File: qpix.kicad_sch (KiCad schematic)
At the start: 91 parts, among them J1 Conn_01x40, J10 VC, J13 DigReset, J2 Conn_01x09, J3 Conn_02x03, J4 Conn_02x03, J5 SPI, J6 Conn_02x03, J8 Conn_02x03, J9 Conn_Coaxial_Power, Q1 AO7400, Q2 AO7400, Q3 AO7400, Q4 AO7400, U1 qpix_digital

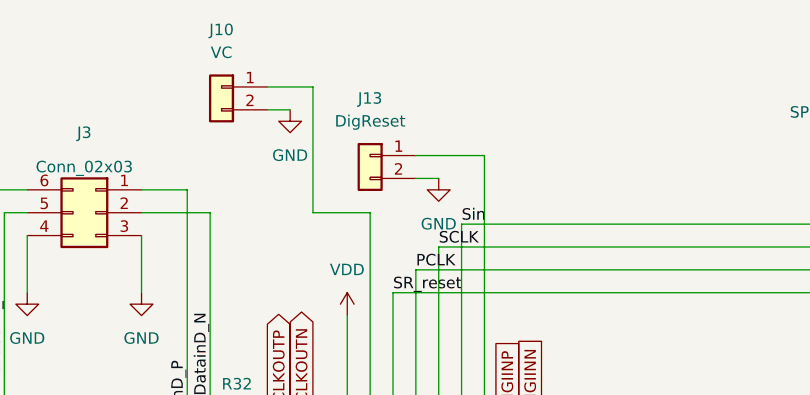
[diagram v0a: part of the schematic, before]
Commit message: clk select related components moved to the top layer
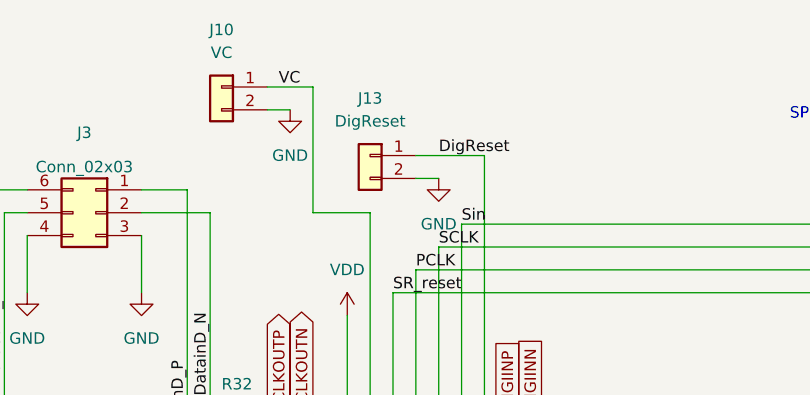
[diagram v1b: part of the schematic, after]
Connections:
- net DigReset: now reaches J13.1 (Pin_1), U1.122 (DigReset)
- net VC: now reaches J10.1 (Pin_1), U1.117 (VC)
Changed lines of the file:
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@@
+    (effects (font (size 1.27 1.27)) (justify left bottom))
+  )
+  (label "DigReset" (at 203.2 31.75 0) (fields_autoplaced)
     (effects (font (size 1.27 1.27)) (justify left bottom))
   )
@@
     (effects (font (size 1.27 1.27)) (justify left bottom))
   )
+  (label "VC" (at 185.42 24.13 0) (fields_autoplaced)
+    (effects (font (size 1.27 1.27)) (justify left bottom))
+  )

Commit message: replace led footprints with 0603, add power up led
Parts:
- D1, D2, D3, D4: footprint LED_SMD:LED_0201_0603Metric -> LED_SMD:LED_0603_1608Metric_Pad1.05x0.95mm_HandSolder
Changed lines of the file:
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@@
       (effects (font (size 1.27 1.27)) (justify right))
     )
-    (property "Footprint" "LED_SMD:LED_0201_0603Metric" (at 388.62 184.15 0)
+    (property "Footprint" "LED_SMD:LED_0603_1608Metric_Pad1.05x0.95mm_HandSolder" (at 388.62 184.15 0)
       (effects (font (size 1.27 1.27)) hide)
     )
@@
       (effects (font (size 1.27 1.27)) (justify right))
     )
-    (property "Footprint" "LED_SMD:LED_0201_0603Metric" (at 374.65 184.15 0)
+    (property "Footprint" "LED_SMD:LED_0603_1608Metric_Pad1.05x0.95mm_HandSolder" (at 374.65 184.15 0)
       (effects (font (size 1.27 1.27)) hide)
     )
@@
       (effects (font (size 1.27 1.27)) (justify right))
     )
-    (property "Footprint" "LED_SMD:LED_0201_0603Metric" (at 359.41 184.15 0)
+    (property "Footprint" "LED_SMD:LED_0603_1608Metric_Pad1.05x0.95mm_HandSolder" (at 359.41 184.15 0)
       (effects (font (size 1.27 1.27)) hide)
     )
@@
       (effects (font (size 1.27 1.27)) (justify right))
     )
-    (property "Footprint" "LED_SMD:LED_0201_0603Metric" (at 344.17 184.15 0)
-      (effects (font (size 1.27 1.27)) hide)
-    )
+    (property "Footprint" "LED_SMD:LED_0603_1608Metric_Pad1.05x0.95mm_HandSolder" (at 344.17 184.15 0)
+      (effects (font (size 1.27 1.27)) hide)
+    )

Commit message: start rework with lvds txrx :
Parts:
- added JP11, JP13: Jumper_2_Open, symbol Jumper:Jumper_2_Open
- added R48: 100, Resistor_SMD:R_0603_1608Metric, symbol Device:R_Small_US
- added U5: FIN1019M, Package_SO:SOIC-14_3.9x8.7mm_P1.27mm, symbol Interface:FIN1019M
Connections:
- net DatinA_N: now also JP11.2 (B), R48.1, U5.11 (DO-); no longer J4.2 (Pin_2)
- net DatinA_P: now also JP13.1 (A), JP13.2 (B), R48.2, U5.12 (DO+), U5.2 (DI)
- net DatoutA_N: no longer J4.6 (Pin_6)
- net DatoutA_P: no longer J4.5 (Pin_5)
- new net: J4.2 (Pin_2), JP11.1 (A)
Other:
- moved on the sheet: J4

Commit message: lvds receiver/driver added for every endeavour port along with 3.3V power supply
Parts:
- removed C22, C23: 100nF, Capacitor_SMD:C_0603_1608Metric, symbol Device:C
- removed J1: Conn_01x40, Connector_PinHeader_2.54mm:PinHeader_2x20_P2.54mm_Vertical, symbol Connector_Generic:Conn_01x40
- removed J2: Conn_01x09, Connector_PinHeader_2.54mm:PinHeader_1x09_P2.54mm_Vertical, symbol Connector_Generic:Conn_01x09
- removed J3, J4, J6, J8: Conn_02x03, Connector_PinSocket_2.54mm:PinSocket_2x03_P2.54mm_Horizontal, symbol Connector_Generic:Conn_02x03_Counter_Clockwise
- removed J9: Conn_Coaxial_Power, Connector_Coaxial:SMA_Amphenol_901-144_Vertical, symbol Connector:Conn_Coaxial_Power
- removed JP10, JP12, JP2, JP3, JP4, JP5, JP6, JP7, JP8, JP9: (no value), Connector_PinHeader_2.54mm:PinHeader_1x02_P2.54mm_Vertical, symbol Jumper:Jumper_2_Open
- removed JP11, JP13: Jumper_2_Open, symbol Jumper:Jumper_2_Open
- removed R1, R11, R12, R2, R3, R4, R5, R6: 10k, Resistor_SMD:R_0603_1608Metric, symbol Device:R_US
- removed R10, R14: 22k, Resistor_SMD:R_0603_1608Metric, symbol Device:R_Small_US
- removed R31, R32, R33, R35, R48: 100, Resistor_SMD:R_0603_1608Metric, symbol Device:R_Small_US
- removed U5: FIN1019M, Package_SO:SOIC-14_3.9x8.7mm_P1.27mm, symbol Interface:FIN1019M
- added C28: C, Capacitor_SMD:C_0603_1608Metric, symbol Device:C
- added R50, R67: NC, Resistor_SMD:R_0805_2012Metric_Pad1.20x1.40mm_HandSolder, symbol Device:R_Small_US
- added R54, R58, R62, R66: 100, Resistor_SMD:R_0805_2012Metric_Pad1.20x1.40mm_HandSolder, symbol Device:R_Small_US
- added R68, R69: 10k, Resistor_SMD:R_0603_1608Metric, symbol Device:R_US
- added SW1: SW_Push, Button_Switch_THT:SW_PUSH_6mm_H5mm, symbol Switch:SW_Push
- added TP1: TestInterr, TestPoint:TestPoint_Loop_D3.80mm_Drill2.0mm, symbol Connector:TestPoint
- added TP3, TP4, TP5, TP6: TestGnd, TestPoint:TestPoint_Loop_D3.80mm_Drill2.0mm, symbol Connector:TestPoint
- Q1, Q2, Q3, Q4: footprint Package_TO_SOT_SMD:SOT-323_SC-70 -> Package_TO_SOT_SMD:SOT-323_SC-70_Handsoldering
- renumbered C4 to C1, C13 to C10, C14 to C11, C15 to C12, C16 to C13, C17 to C14, C18 to C15, C24 to C16, C5 to C2, C6 to C3, C7 to C4, C8 to C5, C9 to C6, C10 to C7, C11 to C8, C12 to C9, J10 to J3, J13 to J4, R15 to R1, R24 to R10, R25 to R11, R26 to R12, R27 to R13, R28 to R14, R29 to R15, R30 to R16, R36 to R17, R37 to R18, R38 to R19, R16 to R2, R39 to R20, R40 to R21, R41 to R22, R42 to R23, R43 to R24, R44 to R25, R45 to R26, R17 to R3, R65 to R32, R66 to R37, R67 to R39, R18 to R4, R68 to R40, R19 to R5, R20 to R6, R21 to R7, R22 to R8, R23 to R9
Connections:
- net CLKDIGIINN: now also R50.2
- net CLKDIGIINP: now also R50.1
- net CLKOUTN: now also R67.1
- net CLKOUTP: now also R67.2
- net DatinA_N: now also R54.1
- net DatinA_P: now also R54.2
- net DatinB_N: now also R58.1
- net DatinB_P: now also R58.2
- net DigReset: now also C28.1, R68.2
- net GND: now also C28.2, R69.2, TP3.1, TP4.1, TP5.1, TP6.1
- net VDD: now also SW1.1
- net dbgInterr: now also TP1.1
- net +5V renamed VCC
- net DatainC_N renamed DatinC_N
- net DatinC_N: now also R62.2
- net DatainC_P renamed DatinC_P
- net DatinC_P: now also R62.1
- net DatainD_N renamed DatinD_N
- net DatinD_N: now also R66.2
- net DatainD_P renamed DatinD_P
- net DatinD_P: now also R66.1
- net DataoutC_N renamed DatoutC_N
- net DataoutC_P renamed DatoutC_P
- net DataoutD_N renamed DatoutD_N
- net DataoutD_P renamed DatoutD_P
- new net: R68.1, R69.1, SW1.2
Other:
- added sheet connectors (connectors.kicad_sch)
- added sheet portA (port.kicad_sch)
- added sheet portB (port.kicad_sch)
- added sheet portC (port.kicad_sch)
- added sheet portD (port.kicad_sch)
- note removed: "10k-22k"
- note removed: "2 22 uF 2 2.2 uf 2 220 nf 2 2nf"
- note removed: "Configuration jumpers"
- note removed: "Enable/disable Endevour transceivers"
- note removed: "Endeavor transceivers scaling factor 3 bits"
- note removed: "External interrogation"
- note removed: "Kurtis: One extra suggestion is that as you connect that output VDD to the chip, you can add some small series resistors (1 Ohm or less) so we can measure current draw on core voltages vs. IO voltages."
- note removed: "Q-Pix reset singnals from analog component"
- note removed: "TODO: add a power LED"
- moved on the sheet: C1, C10, C11, C12, C13, C14, C15, C16, C2, C3, C4, C5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

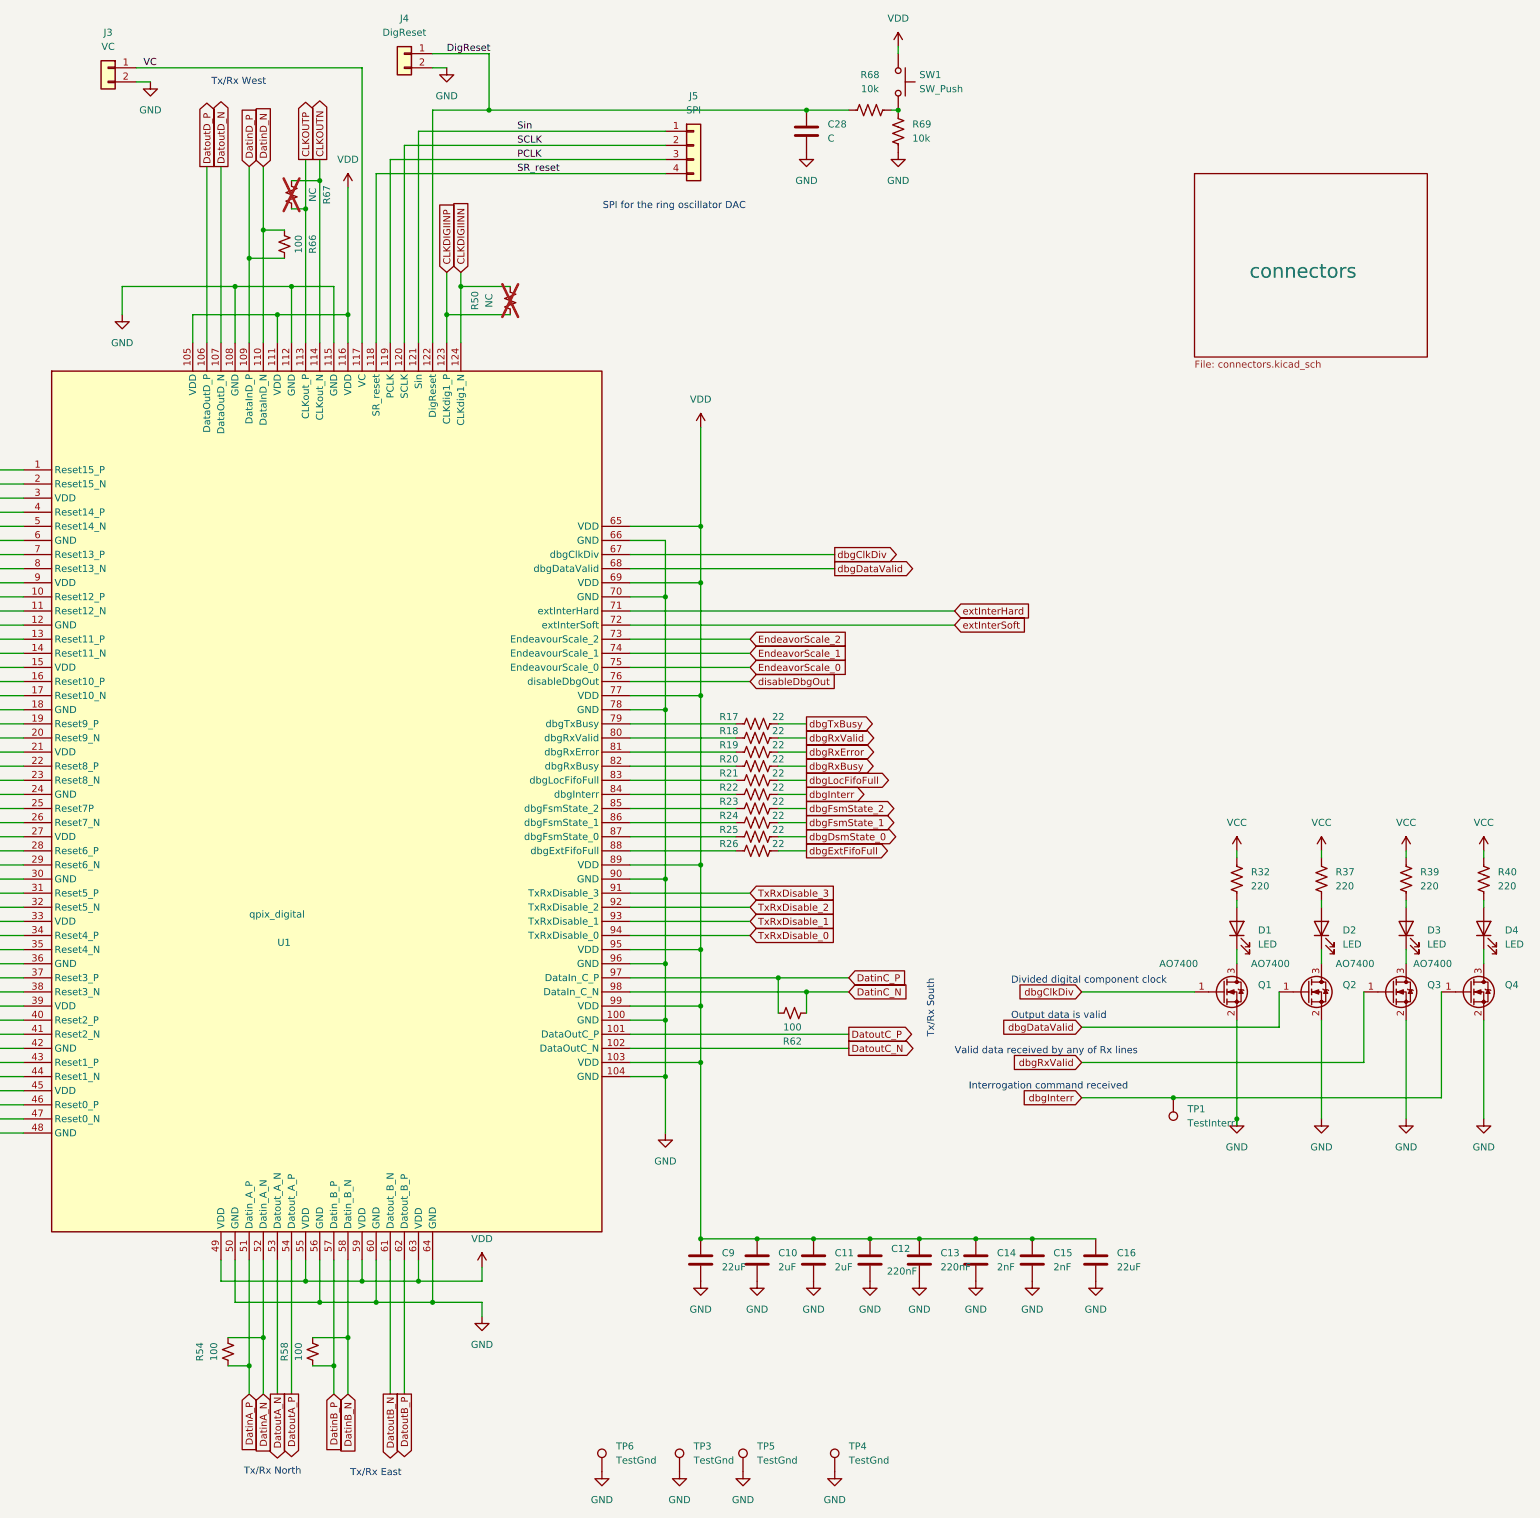
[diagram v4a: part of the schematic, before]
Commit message: add mounting holes, make the board and the zones of rectangular shape, add sikscreen text
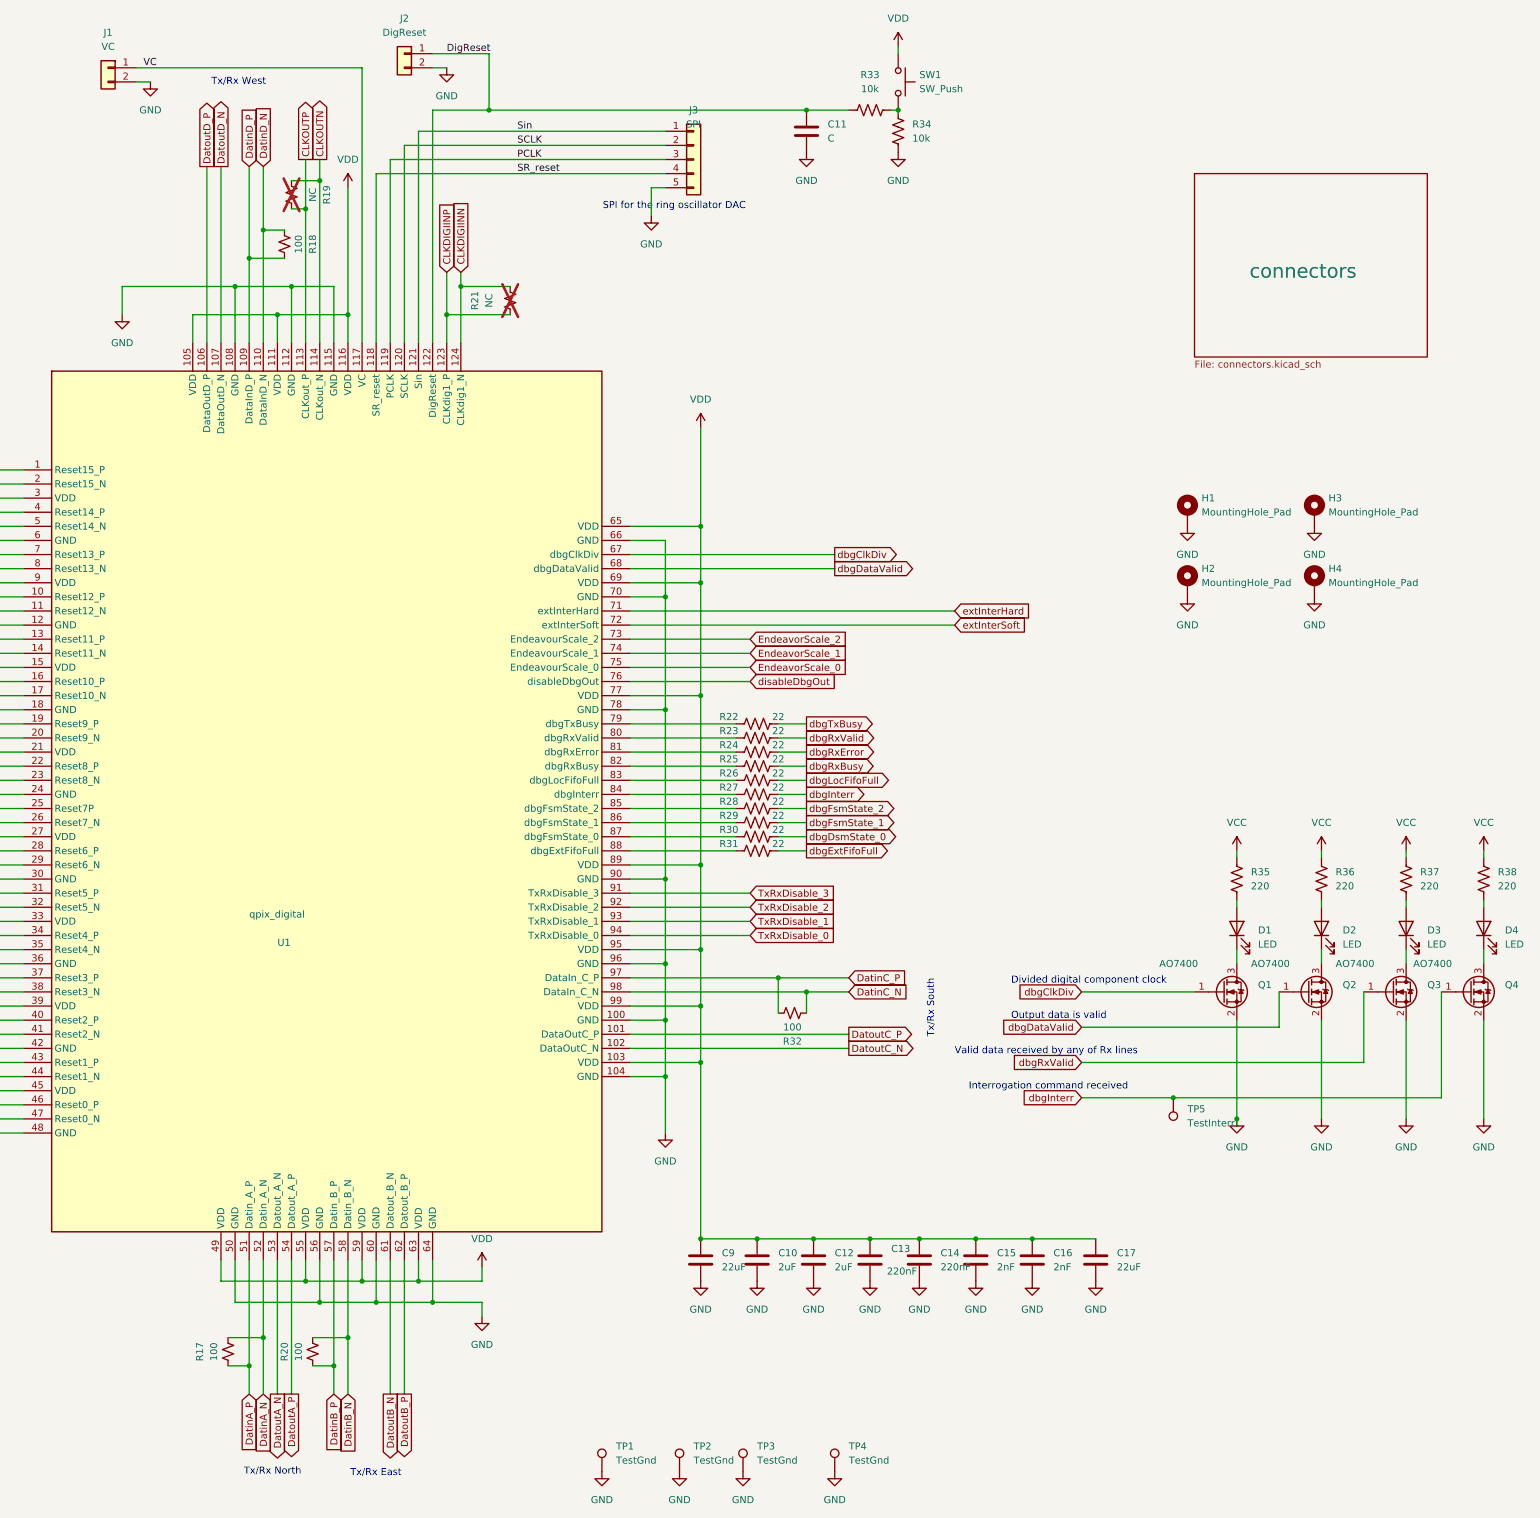
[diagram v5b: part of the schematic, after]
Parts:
- added H1, H2, H3, H4: MountingHole_Pad, MountingHole:MountingHole_3.7mm_Pad_Via, symbol Mechanical:MountingHole_Pad
- J3: renamed from J5; footprint Connector_PinHeader_2.54mm:PinHeader_1x04_P2.54mm_Vertical -> Connector_PinHeader_2.54mm:PinHeader_1x05_P2.54mm_Vertical; symbol Connector_Generic:Conn_01x04 -> Connector_Generic:Conn_01x05
- renumbered C28 to C11, C11 to C12, C12 to C13, C13 to C14, C14 to C15, C15 to C16, C16 to C17, J3 to J1, J4 to J2, R54 to R17, R66 to R18, R67 to R19, R58 to R20, R50 to R21, R17 to R22, R18 to R23, R19 to R24, R20 to R25, R21 to R26, R22 to R27, R23 to R28, R24 to R29, R25 to R30, R26 to R31, R62 to R32, R68 to R33, R69 to R34, R32 to R35, R37 to R36, R39 to R37, R40 to R38, TP6 to TP1, TP3 to TP2, TP5 to TP3, TP1 to TP5
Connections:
- net GND: now also J3.5 (Pin_5), H1.1, H2.1, H3.1, H4.1
